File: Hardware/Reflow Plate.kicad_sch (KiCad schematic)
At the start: 25 parts, among them J3 Conn_02x03_Odd_Even, J4 Conn_02x03_Odd_Even, J5 Conn_02x03_Odd_Even, J6 Conn_02x03_Odd_Even, J7 Conn_01x04_Pin, Q2 Q_NMOS_GDS, SW1 SW_Push, SW2 SW_Push, SW3 SW_Push, SW4 SW_Push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

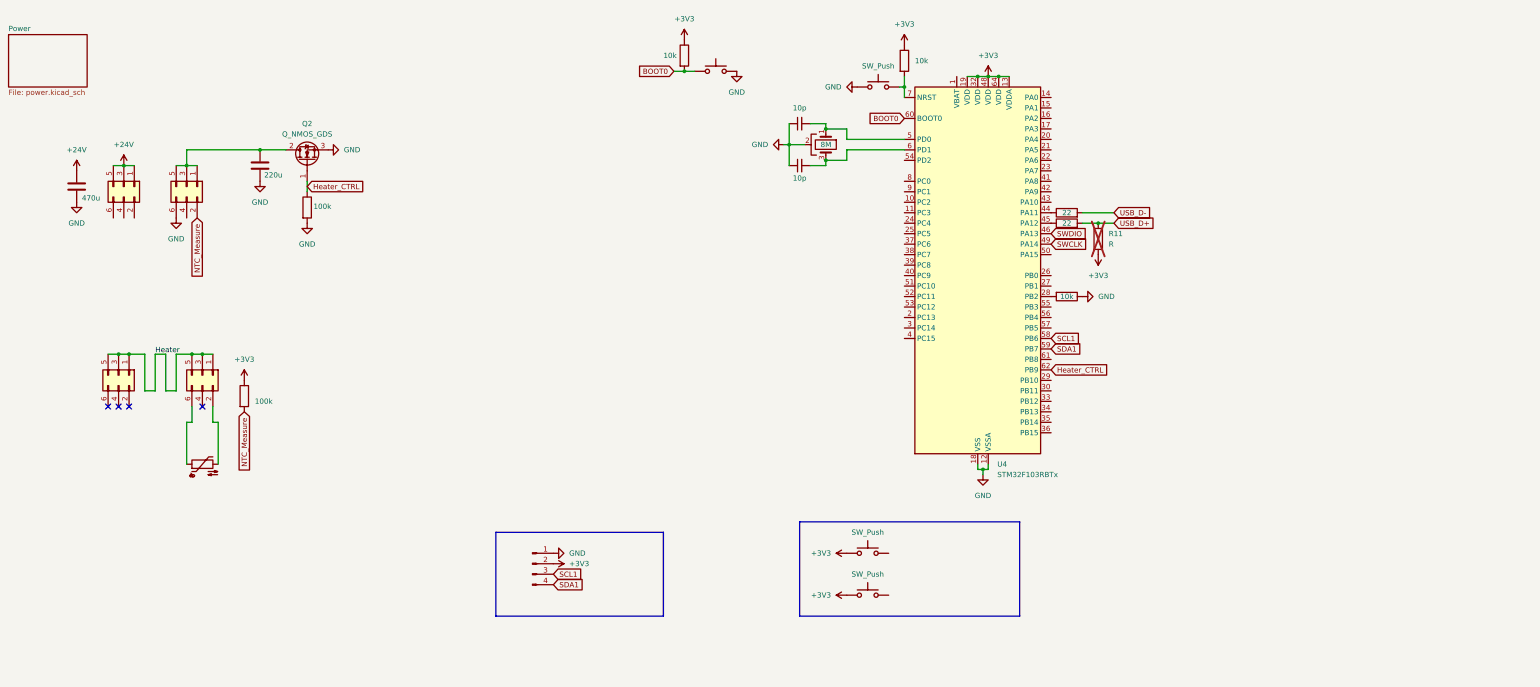
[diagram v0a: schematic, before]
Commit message: Add readme, bad power routing, final heater idea. Likely needs new layout.
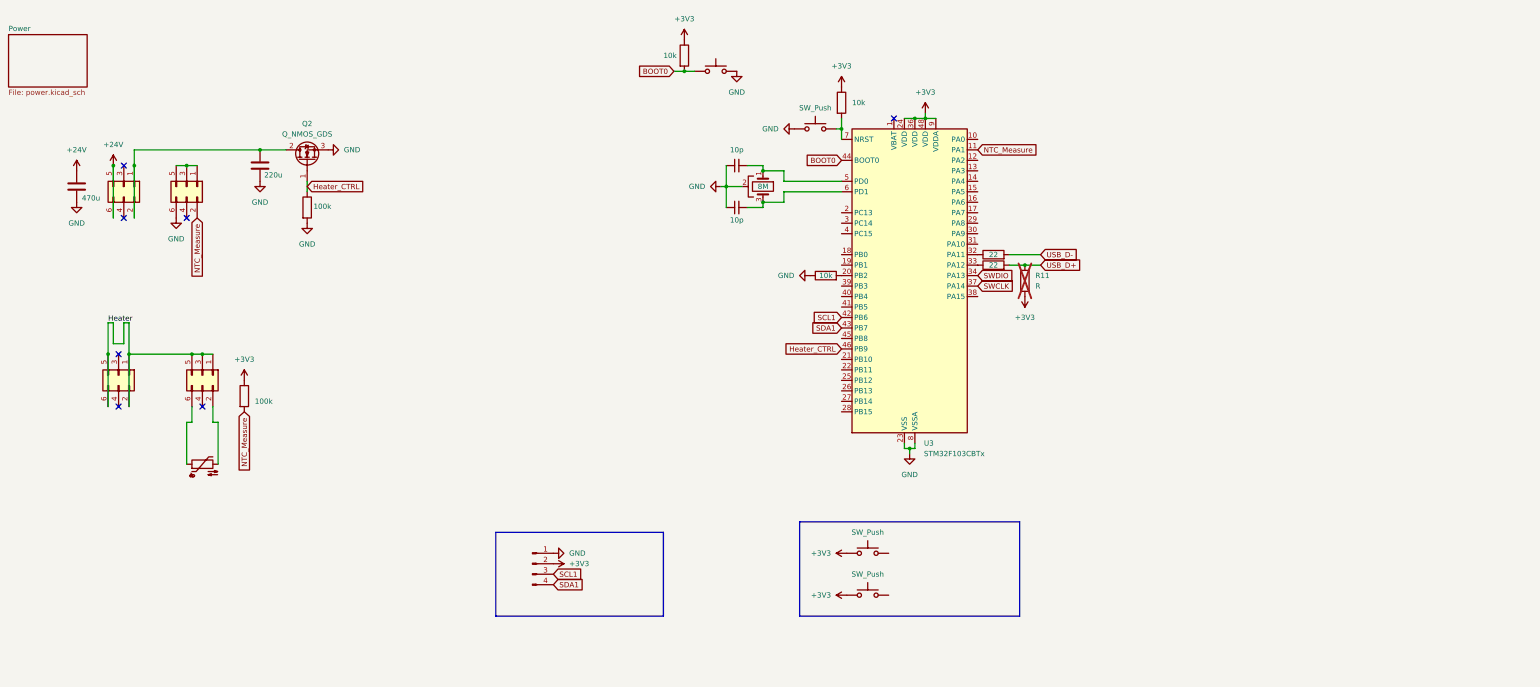
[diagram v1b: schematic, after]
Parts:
- removed U4: STM32F103RBTx, Package_QFP:LQFP-64_10x10mm_P0.5mm, symbol MCU_ST_STM32F1:STM32F103RBTx
- added U3: STM32F103CBTx, Package_QFP:LQFP-48_7x7mm_P0.5mm, symbol MCU_ST_STM32F1:STM32F103CBTx
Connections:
- net +24V: now also J5.6 (Pin_6); no longer J5.1 (Pin_1), J5.3 (Pin_3)
- net +3V3: now also U3.24 (VDD), U3.36 (VDD), U3.48 (VDD), U3.9 (VDDA)
- net BOOT0: now also U3.44 (BOOT0)
- net GND: now also U3.23 (VSS), U3.35 (VSS), U3.47 (VSS), U3.8 (VSSA)
- net Heater: now also J3.2 (Pin_2), J3.6 (Pin_6); no longer J3.3 (Pin_3)
- net Heater_CTRL: now also U3.46 (PB9)
- net NTC_Measure: now also U3.11 (PA1)
- net SCL1: now also U3.42 (PB6)
- net SDA1: now also U3.43 (PB7)
- net SWCLK: now also U3.37 (PA14)
- net SWDIO: now also U3.34 (PA13)
- net at C5.2, Y1.1: now also U3.5 (PD0)
- net at J6.1 (Pin_1), J6.3 (Pin_3), J6.5 (Pin_5): no longer C3.1, Q2.2 (D)
- net at R5.2: now also U3.20 (PB2)
- net at C6.2, Y1.3: now also U3.6 (PD1)
- net at R8.2, SW1.2: now also U3.7 (NRST)
- net at R9.1: now also U3.32 (PA11)
- net at R10.1: now also U3.33 (PA12)
- net at J5.2 (Pin_2): now also C3.1, J5.1 (Pin_1), Q2.2 (D)
- no-connect marks 4 -> 7
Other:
- moved on the sheet: R11

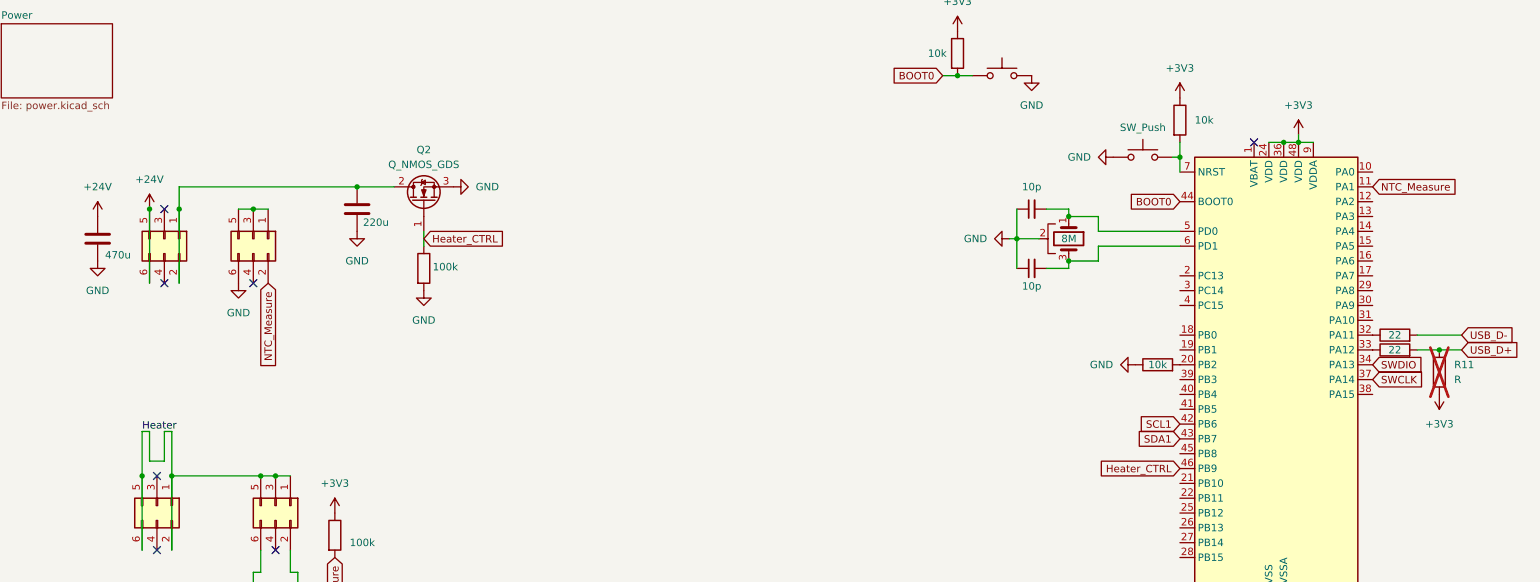
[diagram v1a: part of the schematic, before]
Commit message: Closer to final placement of power components. Shooting for single sided assembly. Still some scuffed placements. Really packed. Missing likely needed ground planes.
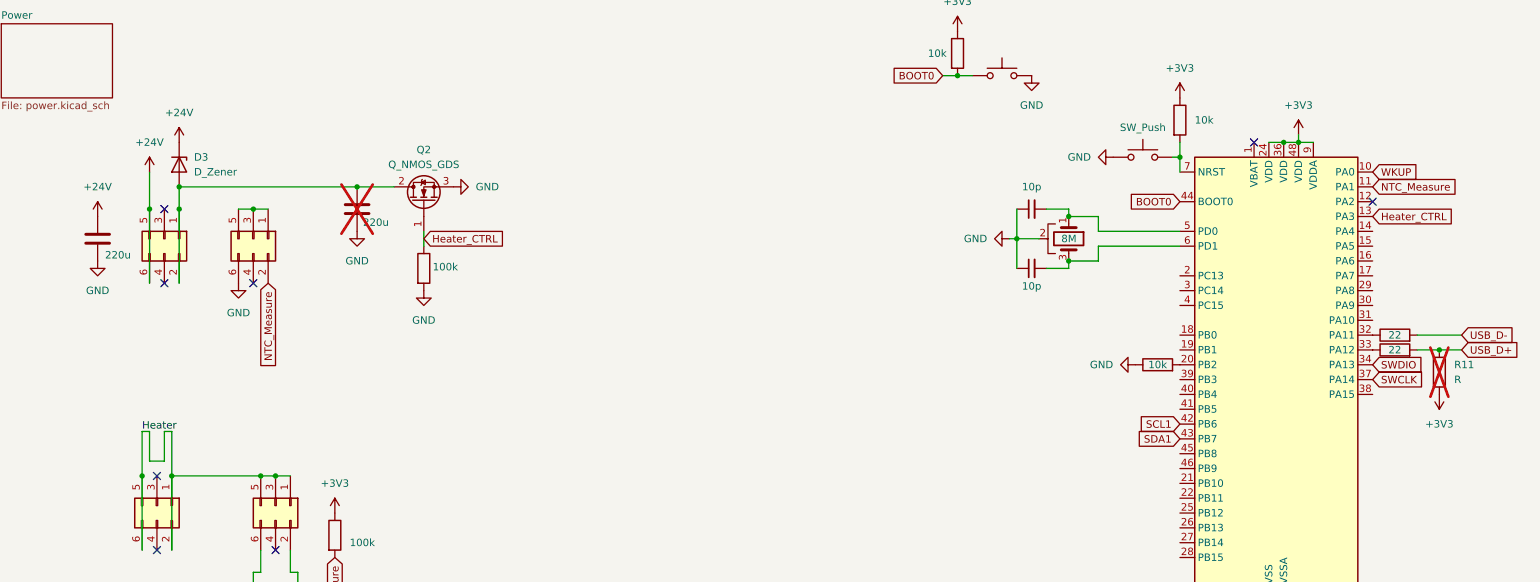
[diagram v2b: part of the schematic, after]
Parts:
- added D3: D_Zener, Diode_SMD:D_SOD-123, symbol Device:D_Zener
- C3: footprint (none) -> Capacitor_SMD:CP_Elec_6.3x7.7; now not fitted; now left out of the parts list
- C4: value 470u -> 220u; footprint (none) -> Capacitor_SMD:CP_Elec_6.3x7.7
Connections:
- net +24V: now also D3.1 (K)
- net Heater_CTRL: now also U3.13 (PA3); no longer U3.46 (PB9)
- net at C3.1, J5.1 (Pin_1), J5.2 (Pin_2)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: now also D3.2 (A)
- net WKUP: now reaches U3.10 (PA0)
- no-connect marks 7 -> 8
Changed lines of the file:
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@@
 	(paper "A4")
 	(junction
+		(at 46.99 46.99)
+		(diameter 0)
+		(color 0 0 0 0)
+	)
+	(junction
 		(at 190.5 55.88)
 		(diameter 0)
@@
 	)
 	(junction
-		(at 63.5 96.52)
+		(at 41.91 50.8)
 		(diameter 0)
 		(color 0 0 0 0)
 	)
 	(junction
-		(at 77.47 46.99)
+		(at 63.5 96.52)
 		(diameter 0)
 		(color 0 0 0 0)
 	)
 	(junction
-		(at 41.91 50.8)
+		(at 77.47 46.99)
 		(diameter 0)
 		(color 0 0 0 0)
@@
 	)
 	(no_connect
+		(at 251.46 49.53)
+	)
+	(no_connect
 		(at 59.69 63.5)
 	)
@@
 	(wire
 		(pts
+			(xy 41.91 44.45) (xy 41.91 50.8)
+		)
+		(stroke
+			(width 0)
+			(type default)
+		)
+	)
+	(wire
+		(pts
 			(xy 195.58 50.8) (xy 199.39 50.8)
 		)
@@
 		)
 	)
+	(global_label "Heater_CTRL"
+		(shape input)
+		(at 251.46 52.07 0)
+		(fields_autoplaced yes)
+		(effects
+			(font
+				(size 1.27 1.27)
+			)
+			(justify left)
+		)
+		(property "Intersheetrefs" "${INTERSHEET_REFS}"
+			(at 266.1171 52.07 0)
+			(effects
+				(font
+					(size 1.27 1.27)
+				)
+				(justify left)
+				(hide yes)
+			)
+		)
+	)
+	(global_label "WKUP"
+		(shape input)
+		(at 251.46 44.45 0)
+		(fields_autoplaced yes)
+		(effects
+			(font
+				(size 1.27 1.27)
+			)
+			(justify left)
+		)
+		(property "Intersheetrefs" "${INTERSHEET_REFS}"
+			(at 259.7671 44.45 0)
+			(effects
+				(font
+					(size 1.27 1.27)
+				)
+				(justify left)
+				(hide yes)
+			)
+		)
+	)
 	(global_label "USB_D-"
 		(shape input)
@@
 		)
 	)
-	(global_label "Heater_CTRL"
-		(shape input)
-		(at 218.44 95.25 180)
-		(fields_autoplaced yes)
-		(effects
-			(font
-				(size 1.27 1.27)
-			)
-			(justify right)
-		)
-		(property "Intersheetrefs" "${INTERSHEET_REFS}"
-			(at 203.7829 95.25 0)
-			(effects
-				(font
-					(size 1.27 1.27)
-				)
-				(justify right)
-				(hide yes)
-			)
-		)
-	)
 	(symbol
 		(lib_id "Connector_Generic:Conn_02x03_Odd_Even")
@@
 	(symbol
 		(lib_id "power:+24V")
-		(at 41.91 50.8 0)
+		(at 41.91 44.45 0)
 		(unit 1)
 		(exclude_from_sim no)
@@
 		(fields_autoplaced yes)
 		(property "Reference" "#PWR013"
-			(at 41.91 54.61 0)
+			(at 41.91 48.26 0)
 			(effects
 				(font
@@
 		)
 		(property "Value" "+24V"
-			(at 41.91 45.72 0)
+			(at 41.91 39.37 0)
 			(effects
 				(font
@@
 		)
 		(property "Footprint" ""
-			(at 41.91 50.8 0)
+			(at 41.91 44.45 0)
 			(effects
 				(font
@@
 		)
 		(property "Datasheet" ""
-			(at 41.91 50.8 0)
+			(at 41.91 44.45 0)
 			(effects
 				(font
@@
 		)
 		(property "Description" "Power symbol creates a global label with name \"+24V\""
-			(at 41.91 50.8 0)
+			(at 41.91 44.45 0)
 			(effects
 				(font
@@
 		(at 77.47 50.8 0)
 		(unit 1)
-		(exclude_from_sim no)
-		(in_bom yes)
-		(on_board yes)
-		(dnp no)
+		(exclude_from_sim yes)
+		(in_bom no)
+		(on_board no)
+		(dnp yes)
 		(property "Reference" "C3"
 			(at 81.28 49.5299 0)
@@
 			)
 		)
-		(property "Footprint" ""
+		(property "Footprint" "Capacitor_SMD:CP_Elec_6.3x7.7"
 			(at 78.4352 54.61 0)
 			(effects
@@
 			)
 		)
-		(property "Value" "470u"
+		(property "Value" "220u"
 			(at 34.29 58.674 0)
 			(effects
@@
 			)
 		)
-		(property "Footprint" ""
+		(property "Footprint" "Capacitor_SMD:CP_Elec_6.3x7.7"
 			(at 33.9852 59.69 0)
 			(effects
@@
 	)
 	(symbol
+		(lib_id "Device:D_Zener")
+		(at 46.99 43.18 270)
+		(unit 1)
+		(exclude_from_sim no)
+		(in_bom yes)
+		(on_board yes)
+		(dnp no)
+		(fields_autoplaced yes)
+		(property "Reference" "D3"
+			(at 49.53 41.9099 90)
+			(effects
+				(font
+					(size 1.27 1.27)
+				)
+				(justify left)
+			)
+		)
+		(property "Value" "D_Zener"
+			(at 49.53 44.4499 90)
+			(effects
+				(font
+					(size 1.27 1.27)
+				)
+				(justify left)
+			)
+		)
+		(property "Footprint" "Diode_SMD:D_SOD-123"
+			(at 46.99 43.18 0)
+			(effects
+				(font
+					(size 1.27 1.27)
+				)
+				(hide yes)
+			)
+		)
+		(property "Datasheet" "~"
+			(at 46.99 43.18 0)
+			(effects
+				(font
+					(size 1.27 1.27)
+				)
+				(hide yes)
+			)
+		)
+		(property "Description" "Zener diode"
+			(at 46.99 43.18 0)
+			(effects
+				(font
+					(size 1.27 1.27)
+				)
+				(hide yes)
+			)
+		)
+		(pin "2"
+		)
+		(pin "1"
+		)
+		(instances
+			(project "Reflow Plate"
+				(path "/49cd4b29-c85a-4a2b-85b7-8d851eb45e3f"
+					(reference "D3")
+					(unit 1)
+				)
+			)
+		)
+	)
+	(symbol
 		(lib_id "Device:R")
 		(at 88.9 60.96 0)
@@
 					(unit 1)
 				)
+			)
+		)
+	)
+	(symbol
+		(lib_id "power:+24V")
+		(at 46.99 39.37 0)
+		(unit 1)
+		(exclude_from_sim no)
+		(in_bom yes)
+		(on_board yes)
+		(dnp no)
+		(fields_autoplaced yes)
+		(property "Reference" "#PWR033"
+			(at 46.99 43.18 0)
+			(effects
+				(font
+					(size 1.27 1.27)
+				)
+				(hide yes)
+			)
+		)
+		(property "Value" "+24V"
+			(at 46.99 34.29 0)
+			(effects
+				(font
+					(size 1.27 1.27)
+				)
+			)
+		)
+		(property "Footprint" ""
+			(at 46.99 39.37 0)
+			(effects
+				(font
+					(size 1.27 1.27)
+				)
+				(hide yes)
+			)
+		)
+		(property "Datasheet" ""
+			(at 46.99 39.37 0)
+			(effects
+				(font
+					(size 1.27 1.27)
+				)
+				(hide yes)
+			)
+		)
+		(property "Description" "Power symbol creates a global label with name \"+24V\""
+			(at 46.99 39.37 0)
+			(effects
+				(font
+					(size 1.27 1.27)
+				)
+				(hide yes)
+			)
+		)
+		(pin "1"
+		)
+		(instances
+			(project "Reflow Plate"
+				(path "/49cd4b29-c85a-4a2b-85b7-8d851eb45e3f"
+					(reference "#PWR033")
+					(unit 1)
+				)

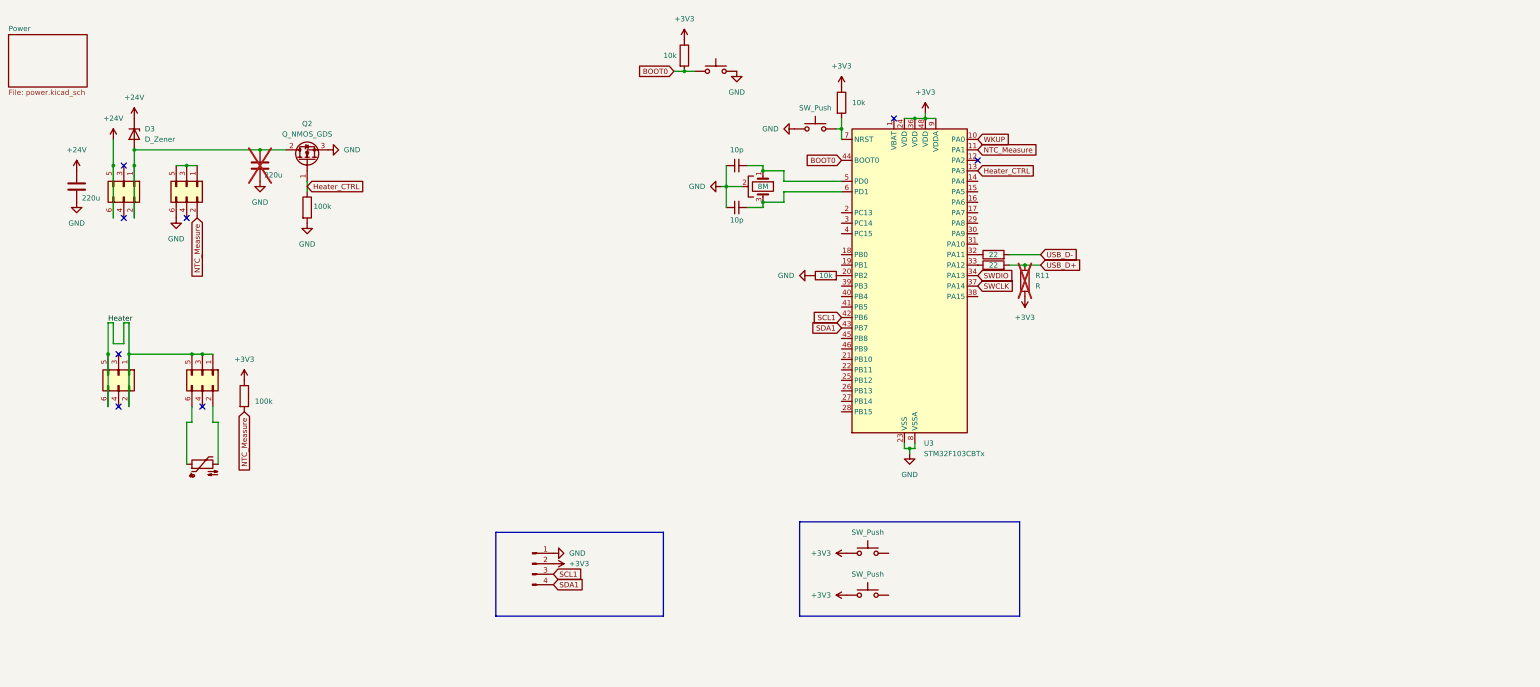
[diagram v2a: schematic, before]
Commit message: Ditch rev 1, moving on to rev 2.
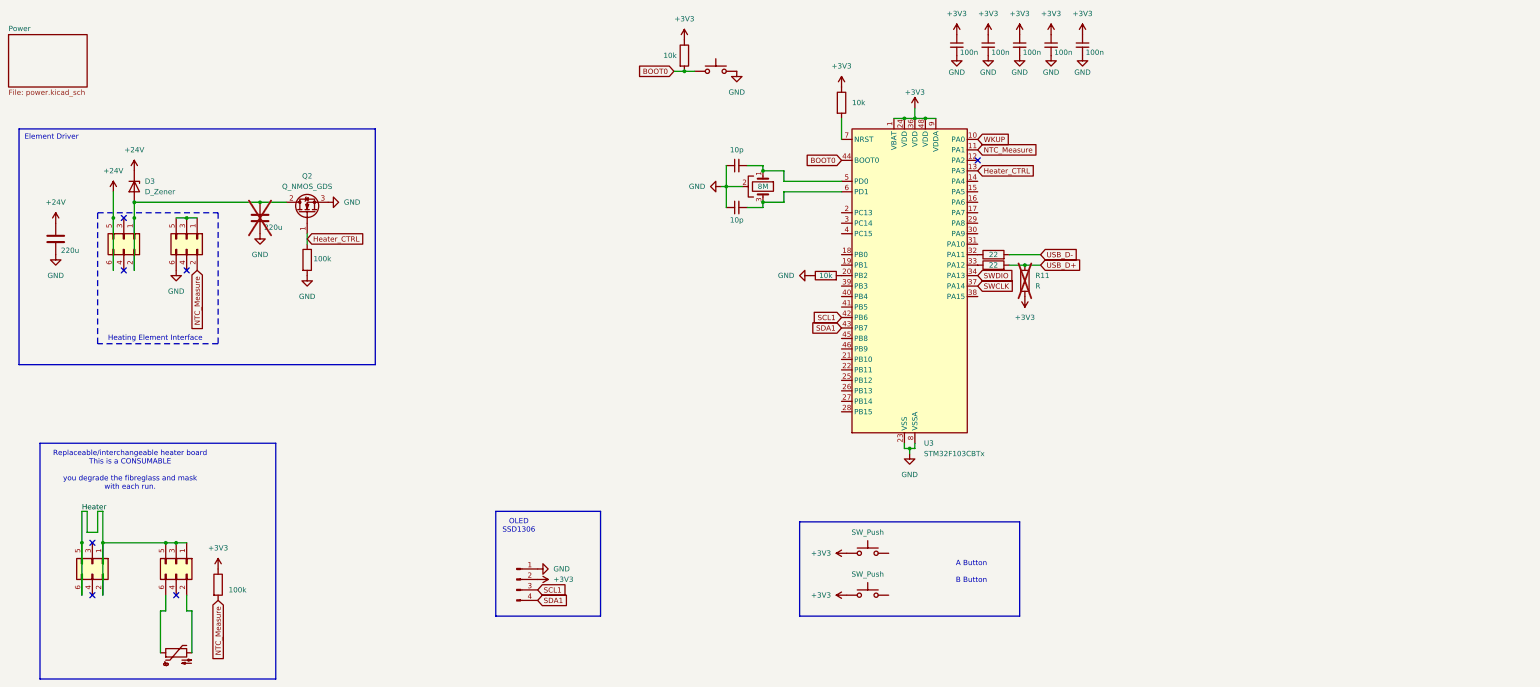
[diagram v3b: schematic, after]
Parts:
- removed SW1: SW_Push, symbol Switch:SW_Push
- added C10, C11, C7, C8, C9: 100n, Capacitor_SMD:C_0402_1005Metric, symbol Device:C_Small
- SW2, SW3, SW4: footprint (none) -> Button_Switch_SMD:SW_Push_1P1T_XKB_TS-1187A
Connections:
- net +3V3: now also U3.1 (VBAT), C10.1, C11.1, C7.1, C8.1, C9.1
- net GND: now also C10.2, C11.2, C7.2, C8.2, C9.2
- no-connect marks 8 -> 7
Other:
- note added: "A Button B Button"
- note added: "Element Driver"
- note added: "Heating Element Interface"
- note added: "OLED SSD1306"
- note added: "Replaceable/interchangeable heater board This is a CONSUMABLE you degrade the fibreglass and mask with each run."
- company: (none) -> Ian Zanath
- title: (none) -> PCB Solder Reflow Plate
- moved on the sheet: D3, Q2
